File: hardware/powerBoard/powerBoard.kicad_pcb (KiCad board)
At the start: 2 copper layers, 65 x 30 mm, 29 parts, among them J1 Batt, J3 Control_Panel, J4 Servo_1, J5 Servo_2, J6 Servo_3, J7 Raspi, J8 Masse, U1 R-78C5.0-1.0, U2 DRV8801PWP

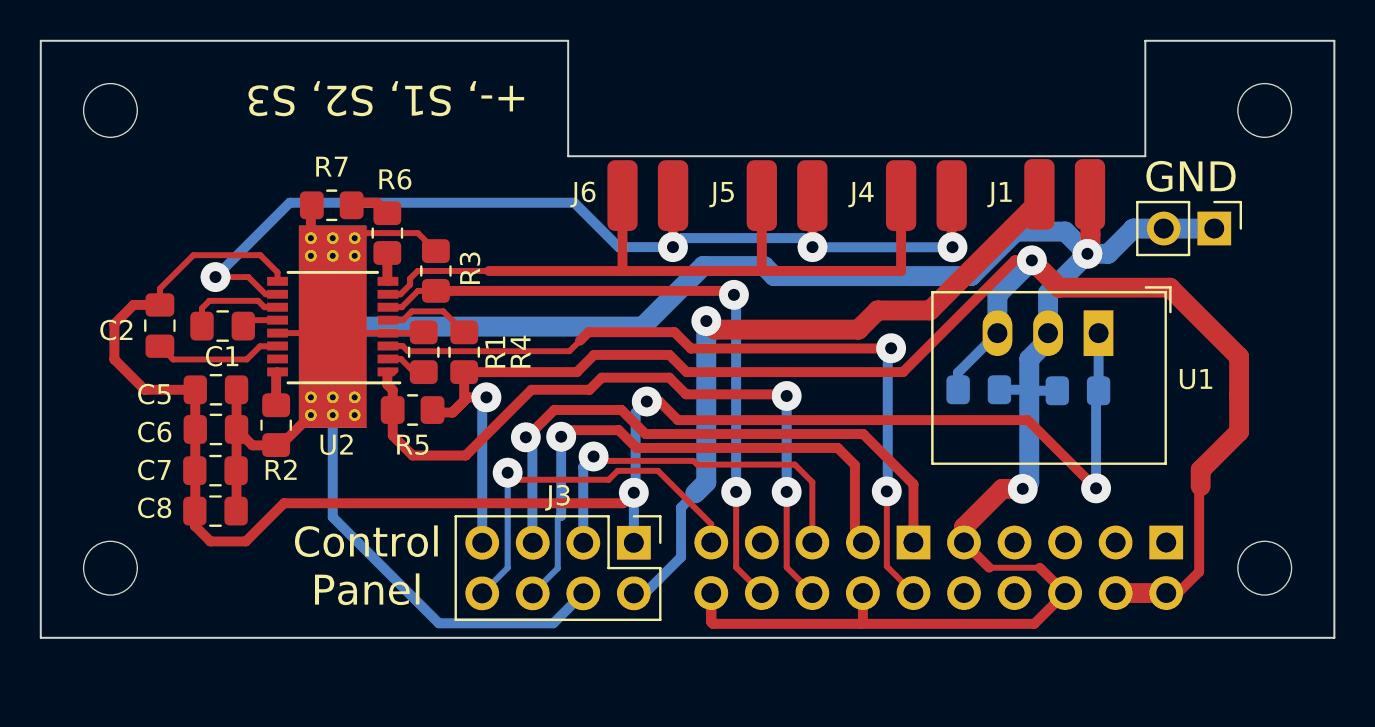
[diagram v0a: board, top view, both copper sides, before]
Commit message: changed the footprint of the connector to the controlPanel and changed the order of the pin numbers
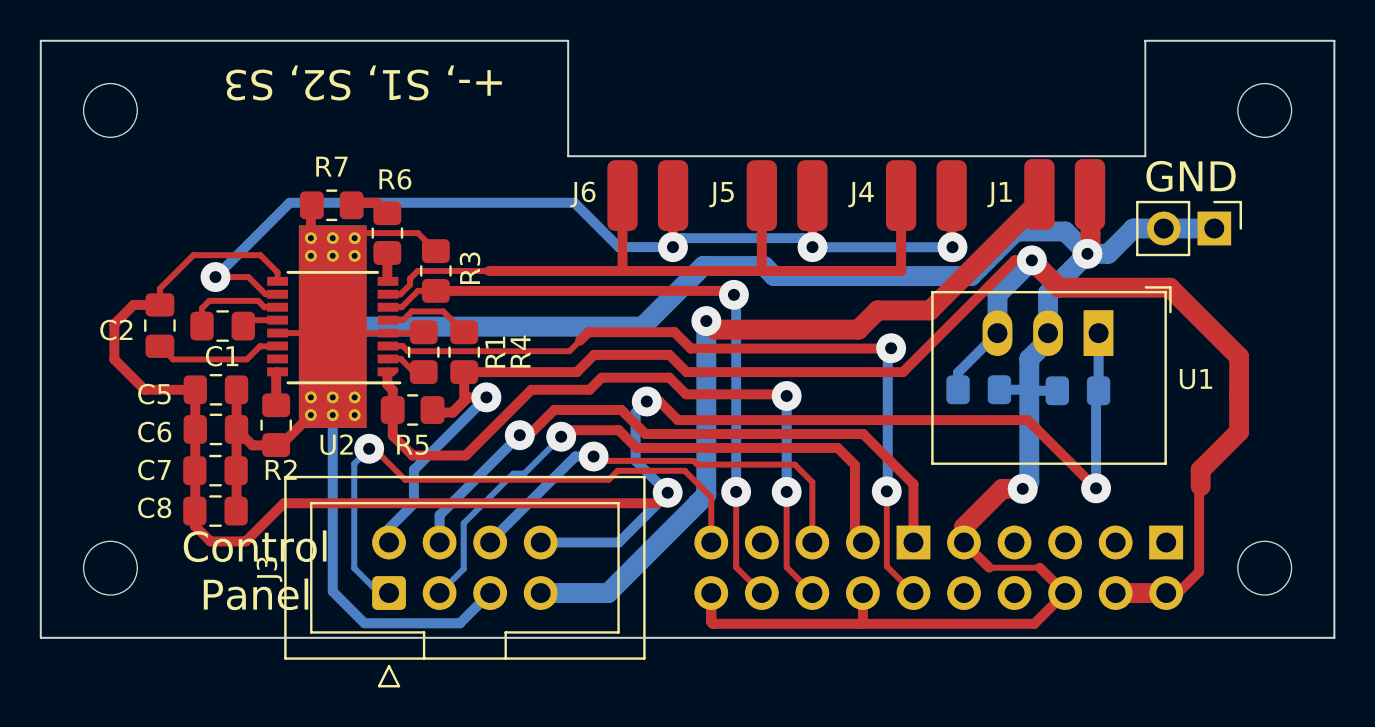
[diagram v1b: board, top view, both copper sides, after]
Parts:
- J3: footprint Connector_PinHeader_2.54mm:PinHeader_2x04_P2.54mm_Vertical -> Connector_IDC:IDC-Header_2x04_P2.54mm_Vertical
- moved J3 12.6 mm to (137.5, 107.8), turned to 90 degrees
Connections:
- J3 pad 1: +12V -> /Button-Pin
- J3 pad 2: /Batt+ -> +5V
- J3 pad 3: /Network-LED -> /BOOT-LED
- J3 pad 4: GND -> /GPS-LED
- J3 pad 5: /GPS-LED -> GND
- J3 pad 6: /BOOT-LED -> /Network-LED
- J3 pad 7: +5V -> /Batt+
- J3 pad 8: /Button-Pin -> +12V
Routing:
- net /Button-Pin: track 19.2 -> 29.4 mm
- net +12V: track 87.2 -> 94.5 mm
- net /Batt+: track 35.4 -> 39.3 mm
- net GND: track 147.9 -> 145.4 mm
- net /Network-LED: track 19.1 -> 21.6 mm
- net /BOOT-LED: track 28.1 -> 30.4 mm
- net +5V: track 81.0 -> 83.0 mm
- net /GPS-LED: track 30.0 -> 31.8 mm
